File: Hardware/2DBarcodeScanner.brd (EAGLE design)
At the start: 44.5 x 25.4 mm, 58 parts, among them Q1 600mA/40V, Q2 600mA/40V, U1 3.3V, U2 BARCODE_SCANNER_MOUNT

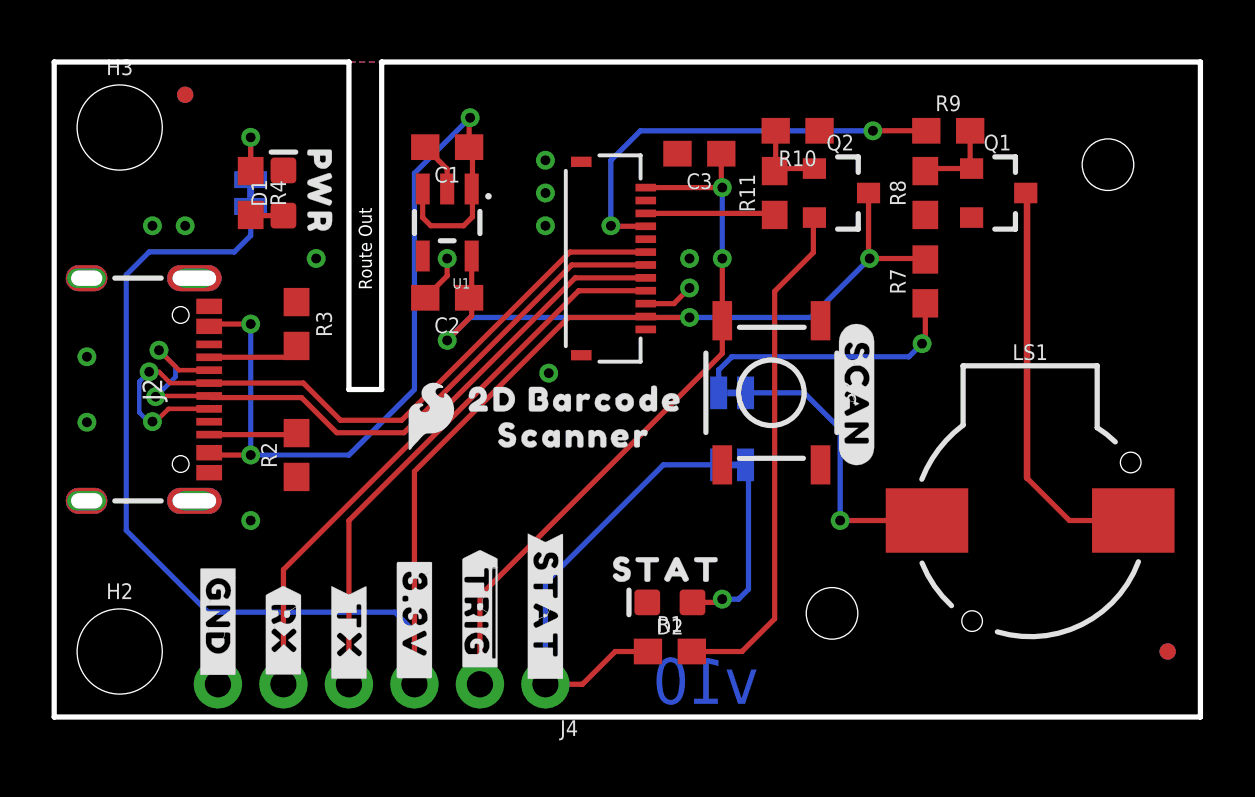
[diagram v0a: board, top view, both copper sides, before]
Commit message: Flip TX and RX pins
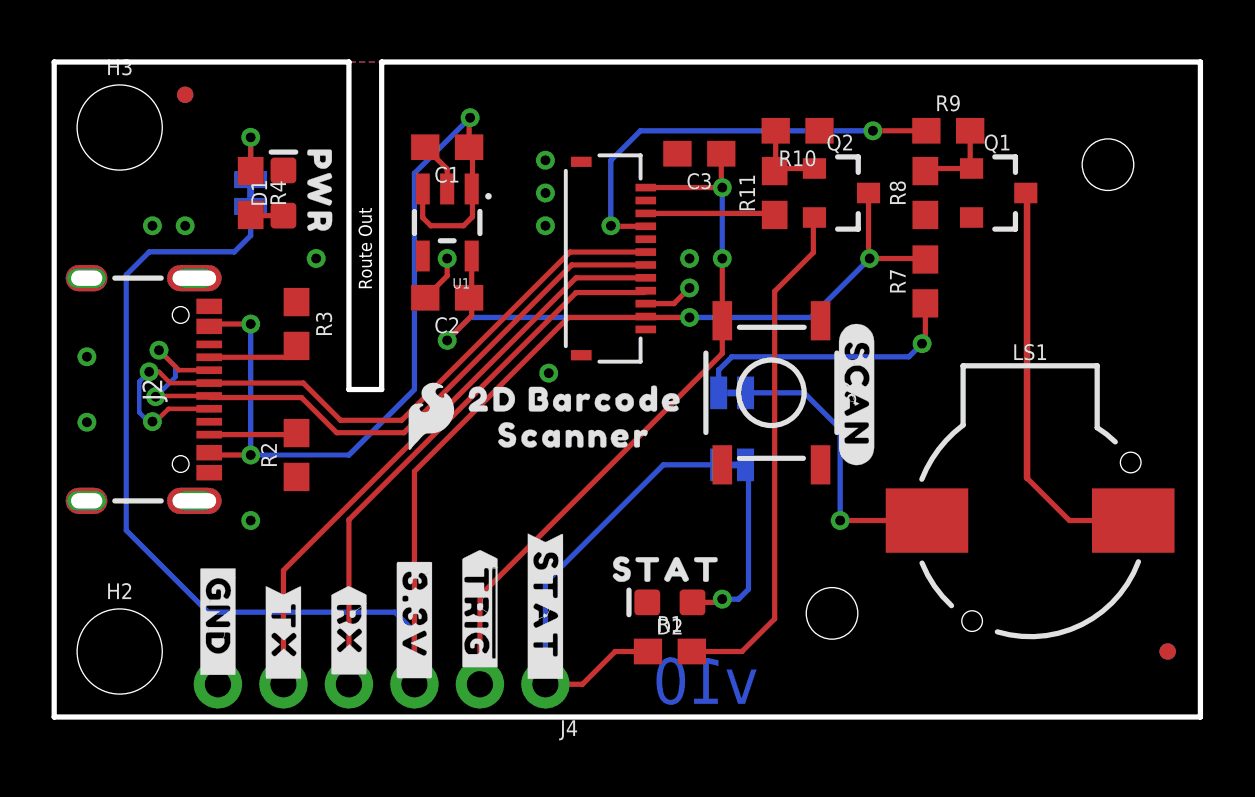
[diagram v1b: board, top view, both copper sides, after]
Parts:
- moved U$26 2.54 mm to (8.89, 5.08)
- moved U$27 2.54 mm to (8.89, 5.08)
- moved U$30 2.54 mm to (11.4, 5.08)
- moved U$31 2.54 mm to (11.4, 5.08)
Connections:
- net RXI: now also J3.9, J4.4; no longer J3.8, J4.5
- net TXO: now also J3.8, J4.5; no longer J3.9, J4.4
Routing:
- net RXI: track 23.2 -> 21.6 mm
- net TXO: track 21.6 -> 23.2 mm
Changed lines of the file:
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@@
 <drawing>
 <settings>
-<setting alwaysvectorfont="no"/>
+<setting alwaysvectorfont="yes"/>
 <setting verticaltext="up"/>
 </settings>
@@
 <layer number="45" name="Holes" color="7" fill="1" visible="yes" active="yes"/>
 <layer number="46" name="Milling" color="3" fill="1" visible="no" active="yes"/>
-<layer number="47" name="Measures" color="7" fill="1" visible="yes" active="yes"/>
+<layer number="47" name="Measures" color="7" fill="1" visible="no" active="yes"/>
 <layer number="48" name="Document" color="7" fill="1" visible="no" active="yes"/>
 <layer number="49" name="Reference" color="7" fill="1" visible="no" active="yes"/>
@@
 <element name="U$28" library="output" package="#3#3V_#0" value="" x="13.97" y="6.35" smashed="yes" rot="R270"/>
 <element name="U$29" library="output" package="#3#3V_#0" value="" x="13.97" y="6.35" smashed="yes" rot="MR270"/>
-<element name="U$26" library="output" package="#TX_#0" value="" x="11.43" y="5.08" smashed="yes" rot="R270"/>
-<element name="U$27" library="output" package="#TX_#0" value="" x="11.43" y="5.08" smashed="yes" rot="MR270"/>
-<element name="U$30" library="output" package="#RX_#0" value="" x="8.89" y="5.08" smashed="yes" rot="R270"/>
-<element name="U$31" library="output" package="#RX_#0" value="" x="8.89" y="5.08" smashed="yes" rot="MR270"/>
+<element name="U$26" library="output" package="#TX_#0" value="" x="8.89" y="5.08" smashed="yes" rot="R270"/>
+<element name="U$27" library="output" package="#TX_#0" value="" x="8.89" y="5.08" smashed="yes" rot="MR270"/>
+<element name="U$30" library="output" package="#RX_#0" value="" x="11.43" y="5.08" smashed="yes" rot="R270"/>
+<element name="U$31" library="output" package="#RX_#0" value="" x="11.43" y="5.08" smashed="yes" rot="MR270"/>
 <element name="U$32" library="output" package="#GND_#0" value="" x="6.35" y="6.096" smashed="yes" rot="R270"/>
 <element name="U$33" library="output" package="#GND_#0" value="" x="6.35" y="6.096" smashed="yes" rot="MR270"/>
@@
 </signal>
 <signal name="TXO">
-<contactref element="J4" pad="4"/>
-<wire x1="20.34" y1="16.53" x2="11.43" y2="7.62" width="0.2032" layer="1"/>
-<wire x1="11.43" y1="7.62" x2="11.43" y2="1.27" width="0.2032" layer="1"/>
-<contactref element="J3" pad="9"/>
-<wire x1="22.94" y1="16.53" x2="20.34" y2="16.53" width="0.2032" layer="1"/>
+<contactref element="J3" pad="8"/>
+<contactref element="J4" pad="5"/>
+<wire x1="8.89" y1="1.27" x2="8.89" y2="5.68418125" width="0.2032" layer="1"/>
+<wire x1="20.23581875" y1="17.03" x2="22.94" y2="17.03" width="0.2032" layer="1"/>
+<wire x1="8.89" y1="5.68418125" x2="20.23581875" y2="17.03" width="0.2032" layer="1"/>
 </signal>
 <signal name="RXI">
-<contactref element="J4" pad="5"/>
-<wire x1="8.89" y1="5.715" x2="8.89" y2="1.27" width="0.2032" layer="1"/>
-<contactref element="J3" pad="8"/>
-<wire x1="20.205" y1="17.03" x2="8.89" y2="5.715" width="0.2032" layer="1"/>
-<wire x1="22.94" y1="17.03" x2="20.205" y2="17.03" width="0.2032" layer="1"/>
+<contactref element="J3" pad="9"/>
+<contactref element="J4" pad="4"/>
+<wire x1="22.94" y1="16.53" x2="22.8694" y2="16.4594" width="0.2032" layer="1"/>
+<wire x1="22.8694" y1="16.4594" x2="20.23858125" y2="16.4594" width="0.2032" layer="1"/>
+<wire x1="20.23858125" y1="16.4594" x2="11.43" y2="7.65081875" width="0.2032" layer="1"/>
+<wire x1="11.43" y1="7.65081875" x2="11.43" y2="1.27" width="0.2032" layer="1"/>
 </signal>
 <signal name="5V">

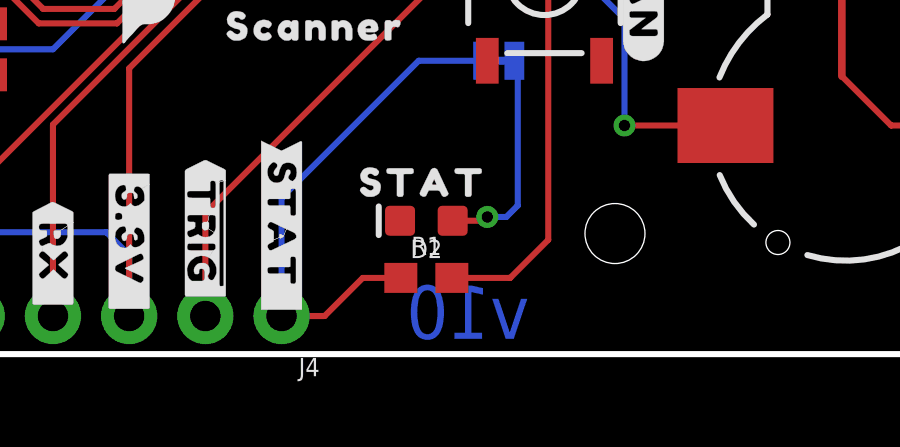
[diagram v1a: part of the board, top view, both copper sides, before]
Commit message: Update version number and re-panelize v11
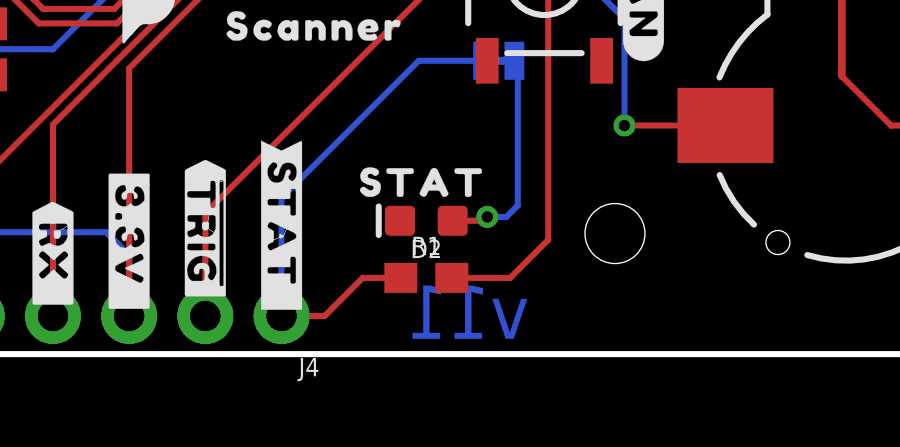
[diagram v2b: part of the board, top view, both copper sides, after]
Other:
- board text added: "v11"
- board text removed: "v10"
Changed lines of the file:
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@@
 <?xml version="1.0" encoding="utf-8"?>
 <!DOCTYPE eagle SYSTEM "eagle.dtd">
-<eagle version="9.5.2">
+<eagle version="9.6.2">
 <drawing>
 <settings>
-<setting alwaysvectorfont="yes"/>
+<setting alwaysvectorfont="no"/>
 <setting verticaltext="up"/>
 </settings>
@@
 Revised by: Priyanka Makin
 </text>
-<text x="27.305" y="0.508" size="1.778" layer="16" font="vector" ratio="15" rot="MR0">v10</text>
+<text x="27.305" y="0.508" size="1.778" layer="16" font="vector" ratio="15" rot="MR0">v11</text>
 <dimension x1="2.54" y1="22.86" x2="2.54" y2="2.54" x3="-2.54" y3="12.7" textsize="1.778" textratio="15" layer="47" unit="inch"/>
 <dimension x1="0" y1="25.4" x2="0" y2="0" x3="-6.35" y3="12.7" textsize="1.778" textratio="15" layer="47" unit="inch"/>

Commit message: Switch status LED from blue to green and change pull-up to 100 ohms
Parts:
- D2: value BLUE -> GREEN
- R1: value 1k -> 100
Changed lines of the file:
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@@
 <?xml version="1.0" encoding="utf-8"?>
 <!DOCTYPE eagle SYSTEM "eagle.dtd">
-<eagle version="9.6.2">
+<eagle version="9.5.2">
 <drawing>
 <settings>
@@
 <element name="U$4" library="output" package="#SCAN#0" value="" x="31.115" y="15.24" smashed="yes" rot="R270"/>
 <element name="U$5" library="output" package="#BUZZ#0" value="" x="25.4" y="12.573" smashed="yes" rot="MR0"/>
-<element name="R1" library="SparkFun-Resistors" package="0603" value="1k" x="23.876" y="2.54" smashed="yes">
+<element name="R1" library="SparkFun-Resistors" package="0603" value="100" x="23.876" y="2.54" smashed="yes">
 <attribute name="NAME" x="23.876" y="3.302" size="0.6096" layer="25" font="vector" ratio="20" align="bottom-center"/>
-<attribute name="PROD_ID" value="RES-07856" x="23.876" y="2.54" size="1.778" layer="27" font="vector" ratio="15" display="off"/>
-<attribute name="VALUE" x="23.876" y="1.778" size="0.6096" layer="27" font="vector" ratio="20" align="top-center"/>
-</element>
-<element name="D2" library="SparkFun-LED" package="LED-0603" value="BLUE" x="23.876" y="4.445" smashed="yes" rot="R180">
+<attribute name="PROD_ID" value="RES-07863" x="23.876" y="2.54" size="1.778" layer="27" font="vector" ratio="15" display="off"/>
+<attribute name="VALUE" value="100" x="23.876" y="1.778" size="0.6096" layer="27" font="vector" ratio="20" align="top-center"/>
+</element>
+<element name="D2" library="SparkFun-LED" package="LED-0603" value="GREEN" x="23.876" y="4.445" smashed="yes" rot="R180">
 <attribute name="NAME" x="23.876" y="3.81" size="0.6096" layer="25" font="vector" ratio="20" rot="R180" align="bottom-center"/>
-<attribute name="PROD_ID" value="DIO-08575" x="23.876" y="4.445" size="1.778" layer="27" font="vector" ratio="15" rot="R180" display="off"/>
-<attribute name="VALUE" x="23.876" y="5.08" size="0.6096" layer="27" font="vector" ratio="20" rot="R180" align="top-center"/>
+<attribute name="PROD_ID" value="DIO-00821" x="23.876" y="4.445" size="1.778" layer="27" font="vector" ratio="15" rot="R180" display="off"/>
+<attribute name="VALUE" value="GREEN" x="23.876" y="5.08" size="0.6096" layer="27" font="vector" ratio="20" rot="R180" align="top-center"/>
 </element>
 <element name="FRAME1" library="SparkFun-Aesthetics" package="CREATIVE_COMMONS" value="FRAME-LETTER" x="1.27" y="-10.16" smashed="yes">

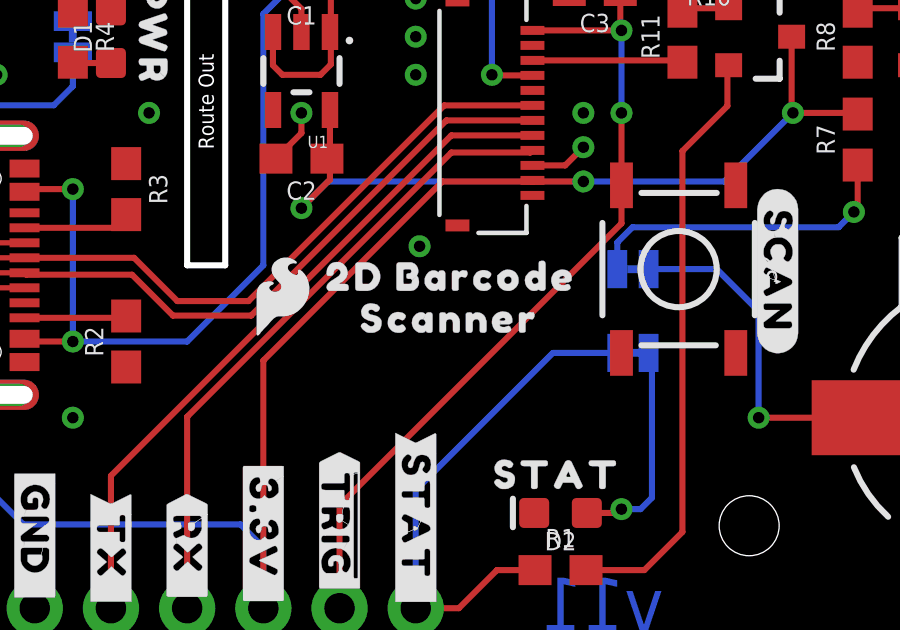
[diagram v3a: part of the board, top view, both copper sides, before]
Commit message: Update silk for V2 board
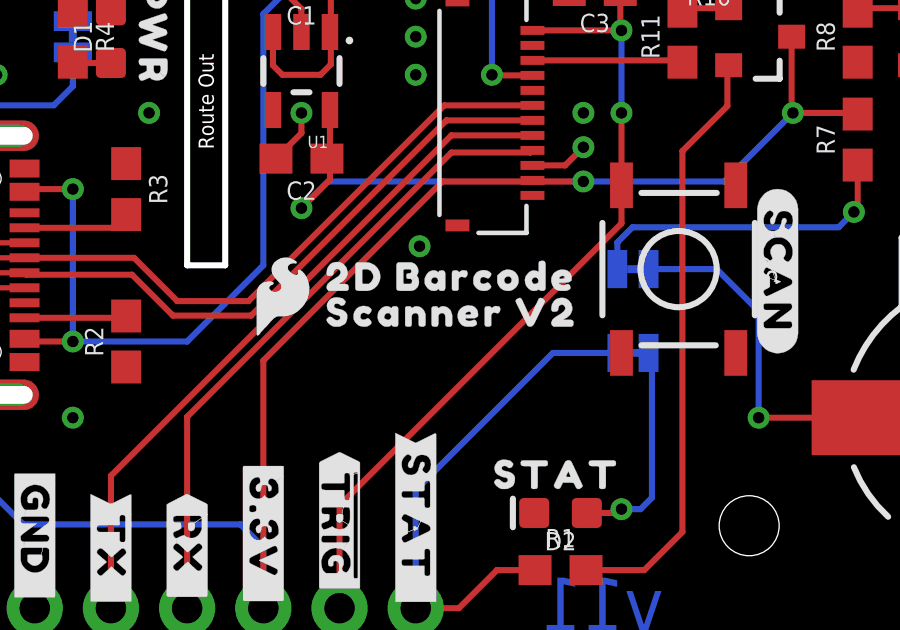
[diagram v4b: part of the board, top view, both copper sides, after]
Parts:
- removed U$18: (no value), output:2D_BARCODE0
- removed U$19: (no value), output:SCANNER0
- removed U$20: (no value), output:SCANNER_BREAKOUT0
- added U$10: (no value), SCANNER_V2:SCANNER_V20
- added U$11: (no value), BREAKOUT_V2:BREAKOUT_V20
- added U$12: (no value), 2D_BARCODE_SCANNER:2D_BARCODE_SCANNER0
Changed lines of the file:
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@@
 <?xml version="1.0" encoding="utf-8"?>
 <!DOCTYPE eagle SYSTEM "eagle.dtd">
-<eagle version="9.5.2">
+<eagle version="9.6.2">
 <drawing>
 <settings>
@@
 <setting verticaltext="up"/>
 </settings>
-<grid distance="0.05" unitdist="inch" unit="inch" style="lines" multiple="1" display="yes" altdistance="0.005" altunitdist="inch" altunit="inch"/>
+<grid distance="12.5" unitdist="mil" unit="mil" style="lines" multiple="1" display="yes" altdistance="12.5" altunitdist="mil" altunit="mil"/>
 <layers>
 <layer number="1" name="Top" color="4" fill="1" visible="yes" active="yes"/>
@@
 <layer number="23" name="tOrigins" color="15" fill="1" visible="yes" active="yes"/>
 <layer number="24" name="bOrigins" color="15" fill="1" visible="yes" active="yes"/>
-<layer number="25" name="tNames" color="7" fill="1" visible="no" active="yes"/>
-<layer number="26" name="bNames" color="7" fill="1" visible="no" active="yes"/>
-<layer number="27" name="tValues" color="7" fill="1" visible="no" active="yes"/>
-<layer number="28" name="bValues" color="7" fill="1" visible="no" active="yes"/>
-<layer number="29" name="tStop" color="7" fill="3" visible="no" active="yes"/>
-<layer number="30" name="bStop" color="7" fill="6" visible="no" active="yes"/>
-<layer number="31" name="tCream" color="7" fill="4" visible="no" active="yes"/>
-<layer number="32" name="bCream" color="7" fill="5" visible="no" active="yes"/>
-<layer number="33" name="tFinish" color="6" fill="3" visible="no" active="yes"/>
-<layer number="34" name="bFinish" color="6" fill="6" visible="no" active="yes"/>
-<layer number="35" name="tGlue" color="7" fill="4" visible="no" active="yes"/>
-<layer number="36" name="bGlue" color="7" fill="5" visible="no" active="yes"/>
-<layer number="37" name="tTest" color="7" fill="1" visible="no" active="yes"/>
-<layer number="38" name="bTest" color="7" fill="1" visible="no" active="yes"/>
-<layer number="39" name="tKeepout" color="4" fill="11" visible="no" active="yes"/>
-<layer number="40" name="bKeepout" color="1" fill="11" visible="no" active="yes"/>
-<layer number="41" name="tRestrict" color="4" fill="10" visible="no" active="yes"/>
-<layer number="42" name="bRestrict" color="1" fill="10" visible="no" active="yes"/>
-<layer number="43" name="vRestrict" color="2" fill="10" visible="no" active="yes"/>
-<layer number="44" name="Drills" color="7" fill="1" visible="no" active="yes"/>
+<layer number="25" name="tNames" color="7" fill="1" visible="yes" active="yes"/>
+<layer number="26" name="bNames" color="7" fill="1" visible="yes" active="yes"/>
+<layer number="27" name="tValues" color="7" fill="1" visible="yes" active="yes"/>
+<layer number="28" name="bValues" color="7" fill="1" visible="yes" active="yes"/>
+<layer number="29" name="tStop" color="7" fill="3" visible="yes" active="yes"/>
+<layer number="30" name="bStop" color="7" fill="6" visible="yes" active="yes"/>
+<layer number="31" name="tCream" color="7" fill="4" visible="yes" active="yes"/>
+<layer number="32" name="bCream" color="7" fill="5" visible="yes" active="yes"/>
+<layer number="33" name="tFinish" color="6" fill="3" visible="yes" active="yes"/>
+<layer number="34" name="bFinish" color="6" fill="6" visible="yes" active="yes"/>
+<layer number="35" name="tGlue" color="7" fill="4" visible="yes" active="yes"/>
+<layer number="36" name="bGlue" color="7" fill="5" visible="yes" active="yes"/>
+<layer number="37" name="tTest" color="7" fill="1" visible="yes" active="yes"/>
+<layer number="38" name="bTest" color="7" fill="1" visible="yes" active="yes"/>
+<layer number="39" name="tKeepout" color="4" fill="11" visible="yes" active="yes"/>
+<layer number="40" name="bKeepout" color="1" fill="11" visible="yes" active="yes"/>
+<layer number="41" name="tRestrict" color="4" fill="10" visible="yes" active="yes"/>
+<layer number="42" name="bRestrict" color="1" fill="10" visible="yes" active="yes"/>
+<layer number="43" name="vRestrict" color="2" fill="10" visible="yes" active="yes"/>
+<layer number="44" name="Drills" color="7" fill="1" visible="yes" active="yes"/>
 <layer number="45" name="Holes" color="7" fill="1" visible="yes" active="yes"/>
-<layer number="46" name="Milling" color="3" fill="1" visible="no" active="yes"/>
-<layer number="47" name="Measures" color="7" fill="1" visible="no" active="yes"/>
-<layer number="48" name="Document" color="7" fill="1" visible="no" active="yes"/>
-<layer number="49" name="Reference" color="7" fill="1" visible="no" active="yes"/>
-<layer number="50" name="dxf" color="7" fill="1" visible="no" active="yes"/>
+<layer number="46" name="Milling" color="3" fill="1" visible="yes" active="yes"/>
+<layer number="47" name="Measures" color="7" fill="1" visible="yes" active="yes"/>
+<layer number="48" name="Document" color="7" fill="1" visible="yes" active="yes"/>
+<layer number="49" name="Reference" color="7" fill="1" visible="yes" active="yes"/>
+<layer number="50" name="dxf" color="7" fill="1" visible="yes" active="yes"/>
 <layer number="51" name="tDocu" color="6" fill="1" visible="yes" active="yes"/>
-<layer number="52" name="bDocu" color="7" fill="1" visible="no" active="yes"/>
+<layer number="52" name="bDocu" color="7" fill="1" visible="yes" active="yes"/>
 <layer number="91" name="Nets" color="2" fill="1" visible="no" active="no"/>
 <layer number="92" name="Busses" color="1" fill="1" visible="no" active="no"/>
@@
 <element name="U$3" library="output" package="STAT0" value="" x="20.955" y="5.715" smashed="yes"/>
 <element name="U$17" library="output" package="2D_BARCODE0" value="" x="15.367" y="12.319" smashed="yes"/>
-<element name="U$18" library="output" package="2D_BARCODE0" value="" x="24.892" y="19.939" smashed="yes" rot="MR0"/>
-<element name="U$20" library="output" package="SCANNER_BREAKOUT0" value="" x="27.432" y="18.542" smashed="yes" rot="MR0"/>
-<element name="U$19" library="output" package="SCANNER0" value="" x="16.51" y="10.922" smashed="yes"/>
 <element name="U$21" library="output" package="#STAT_#0" value="" x="19.05" y="7.112" smashed="yes" rot="MR270"/>
 <element name="U$28" library="output" package="#3#3V_#0" value="" x="13.97" y="6.35" smashed="yes" rot="R270"/>
@@
 <element name="U$1" library="output" package="##TRIG##0" value="" x="16.51" y="6.477" smashed="yes" rot="R270"/>
 <element name="U$7" library="output" package="##TRIG##0" value="" x="16.51" y="6.477" smashed="yes" rot="MR270"/>
+<element name="U$10" library="SCANNER_V2" package="SCANNER_V20" value="" x="15.367" y="11.1252" smashed="yes"/>
+<element name="U$11" library="BREAKOUT_V2" package="BREAKOUT_V20" value="" x="25.4" y="18.415" smashed="yes" rot="MR0"/>
+<element name="U$12" library="2D_BARCODE_SCANNER" package="2D_BARCODE_SCANNER0" value="" x="28.067" y="19.685" smashed="yes" rot="MR0"/>
 </elements>
 <signals>
